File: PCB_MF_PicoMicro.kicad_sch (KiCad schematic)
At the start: 4 parts, among them J2 Conn_01x02_Pin, J7 Conn_01x02_Pin, J8 Conn_01x02_Pin, U5 ProMicro

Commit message: first changes for RP2350A
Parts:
- removed J2: Conn_01x02_Pin, Connector_JST:JST_XH_B2B-XH-A_1x02_P2.50mm_Vertical, symbol _MobiFlight:JST-XH_02_Pin_vertical

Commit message: optimazations
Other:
- sheet RP2040 renamed RP2350A
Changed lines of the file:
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@@
 			(color 0 0 0 0.0000)
 		)
-		(property "Sheetname" "RP2040"
+		(property "Sheetname" "RP2350A"
 			(at 27.94 33.5784 0)
 			(effects

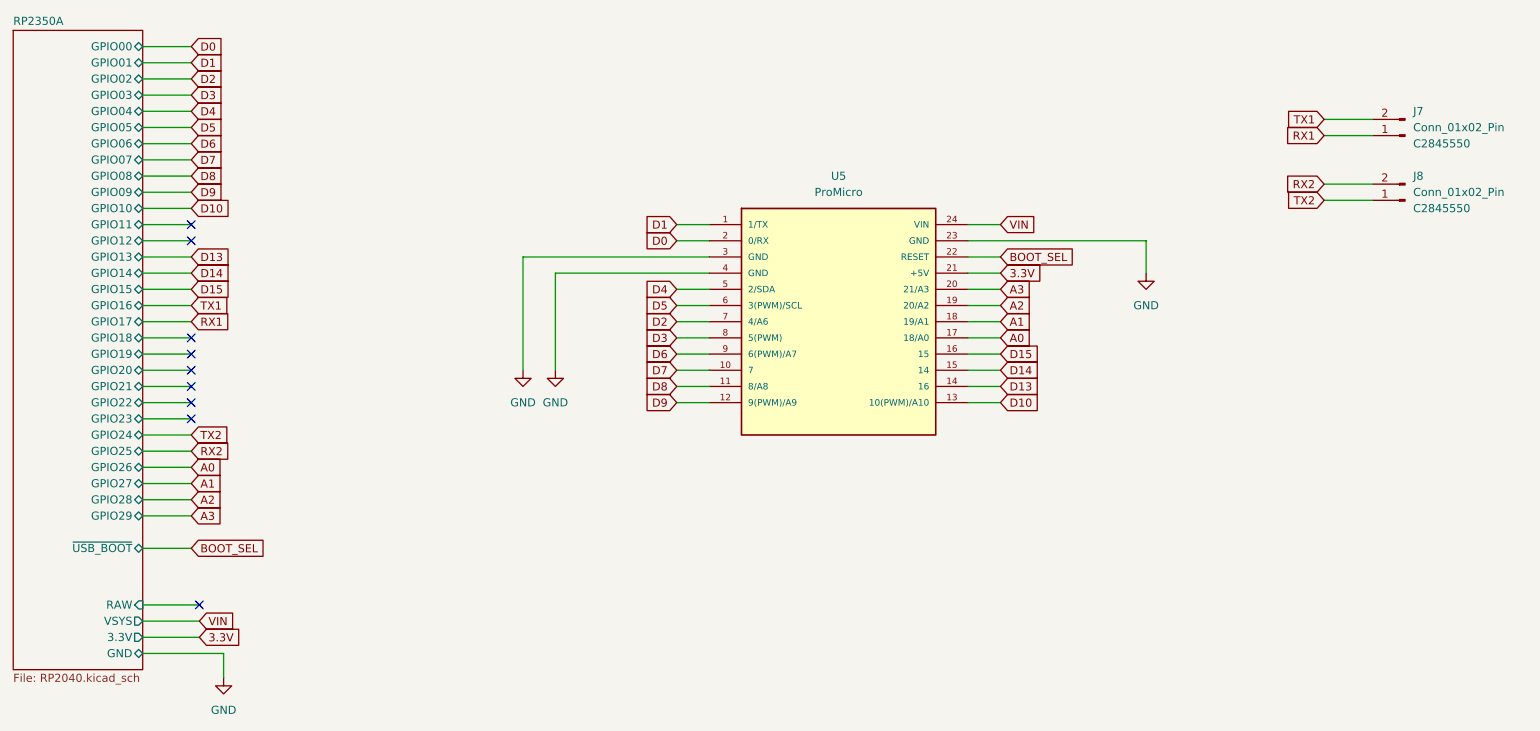
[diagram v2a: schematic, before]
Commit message: add LED, make board smaller
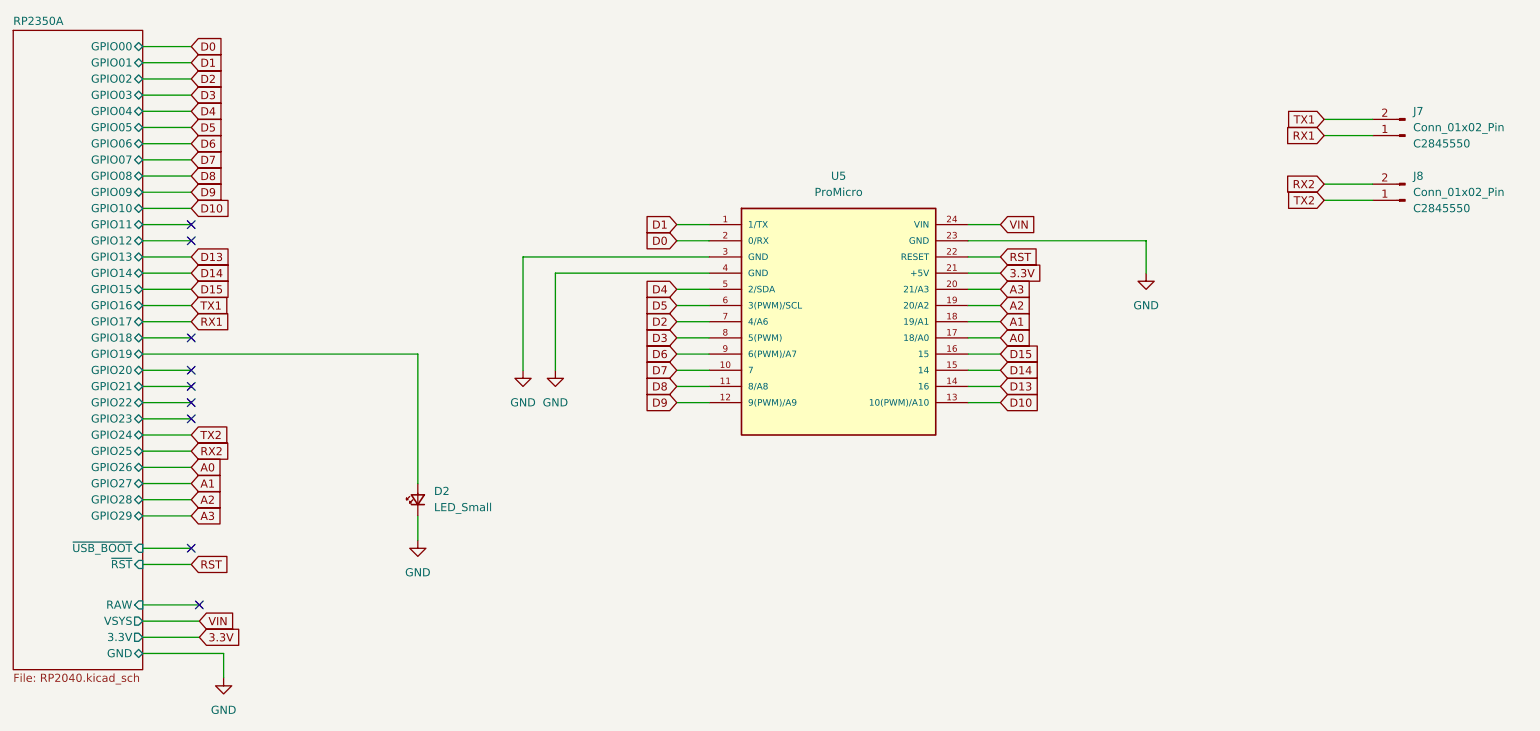
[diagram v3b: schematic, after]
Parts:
- added D2: LED_Small, LED_SMD:LED_0402_1005Metric, symbol Device:LED_Small
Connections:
- net GND: now also D2.1 (K)
- net RP2350A/GPIO19: now also D2.2 (A)
- net BOOT_SEL renamed RST
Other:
- sheet RP2350A ports: added ~{RST}; removed none
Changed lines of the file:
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@@
-	)
-	(no_connect
-		(at 55.88 85.09)
 	)
 	(no_connect
@@
 	)
 	(no_connect
+		(at 55.88 115.57)
+	)
+	(no_connect
 		(at 55.88 92.71)
 	)
@@
 	(wire
 		(pts
+			(xy 91.44 110.49) (xy 91.44 114.3)
+		)
+		(stroke
+			(width 0)
+			(type default)
+		)
+	)
+	(wire
+		(pts
 			(xy 113.03 72.39) (xy 137.16 72.39)
 		)
@@
 	(wire
 		(pts
+			(xy 91.44 85.09) (xy 91.44 105.41)
+		)
+		(stroke
+			(width 0)
+			(type default)
+		)
+	)
+	(wire
+		(pts
 			(xy 48.26 41.91) (xy 55.88 41.91)
 		)
@@
 	(wire
 		(pts
-			(xy 48.26 85.09) (xy 55.88 85.09)
+			(xy 48.26 85.09) (xy 91.44 85.09)
 		)
 		(stroke
@@
 		)
 	)
+	(wire
+		(pts
+			(xy 48.26 118.11) (xy 55.88 118.11)
+		)
+		(stroke
+			(width 0)
+			(type default)
+		)
+	)
 	(global_label "D5"
 		(shape input)
@@
 		)
 	)
+	(global_label "RST"
+		(shape input)
+		(at 55.88 118.11 0)
+		(fields_autoplaced yes)
+		(effects
+			(font
+				(size 1.27 1.27)
+			)
+			(justify left)
+		)
+		(property "Intersheetrefs" "${INTERSHEET_REFS}"
+			(at 62.3123 118.11 0)
+			(effects
+				(font
+					(size 1.27 1.27)
+				)
+				(justify left)
+				(hide yes)
+			)
+		)
+	)
 	(global_label "D7"
 		(shape input)
@@
 		)
 	)
-	(global_label "BOOT_SEL"
-		(shape input)
-		(at 55.88 115.57 0)
-		(fields_autoplaced yes)
-		(effects
-			(font
-				(size 1.27 1.27)
-			)
-			(justify left)
-		)
-		(property "Intersheetrefs" "${INTERSHEET_REFS}"
-			(at 68.118 115.57 0)
-			(effects
-				(font
-					(size 1.27 1.27)
-				)
-				(justify left)
-				(hide yes)
-			)
-		)
-	)
 	(global_label "RX2"
 		(shape input)
@@
 		)
 	)
-	(global_label "BOOT_SEL"
+	(global_label "RST"
 		(shape input)
 		(at 182.88 69.85 0)
@@
 		)
 		(property "Intersheetrefs" "${INTERSHEET_REFS}"
-			(at 195.118 69.85 0)
+			(at 189.3123 69.85 0)
 			(effects
 				(font
@@
 	)
 	(symbol
+		(lib_id "power:GND")
+		(at 91.44 114.3 0)
+		(unit 1)
+		(exclude_from_sim no)
+		(in_bom yes)
+		(on_board yes)
+		(dnp no)
+		(fields_autoplaced yes)
+		(property "Reference" "#PWR017"
+			(at 91.44 120.65 0)
+			(effects
+				(font
+					(size 1.27 1.27)
+				)
+				(hide yes)
+			)
+		)
+		(property "Value" "GND"
+			(at 91.44 119.38 0)
+			(effects
+				(font
+					(size 1.27 1.27)
+				)
+			)
+		)
+		(property "Footprint" ""
+			(at 91.44 114.3 0)
+			(effects
+				(font
+					(size 1.27 1.27)
+				)
+				(hide yes)
+			)
+		)
+		(property "Datasheet" ""
+			(at 91.44 114.3 0)
+			(effects
+				(font
+					(size 1.27 1.27)
+				)
+				(hide yes)
+			)
+		)
+		(property "Description" "Power symbol creates a global label with name \"GND\" , ground"
+			(at 91.44 114.3 0)
+			(effects
+				(font
+					(size 1.27 1.27)
+				)
+				(hide yes)
+			)
+		)
+		(pin "1"
+		)
+		(instances
+			(project "PCB_MF_PicoMicro"
+				(path "/e63e39d7-6ac0-4ffd-8aa3-1841a4541b55"
+					(reference "#PWR017")
+					(unit 1)
+				)
+			)
+		)
+	)
+	(symbol
 		(lib_id "_Own_Library:Conn_01x02_JST_ZH")
 		(at 246.38 60.96 180)
@@
 				(path "/e63e39d7-6ac0-4ffd-8aa3-1841a4541b55"
 					(reference "J8")
+					(unit 1)
+				)
+			)
+		)
+	)
+	(symbol
+		(lib_id "Device:LED_Small")
+		(at 91.44 107.95 90)
+		(unit 1)
+		(exclude_from_sim no)
+		(in_bom yes)
+		(on_board yes)
+		(dnp no)
+		(fields_autoplaced yes)
+		(property "Reference" "D2"
+			(at 93.98 106.6164 90)
+			(effects
+				(font
+					(size 1.27 1.27)
+				)
+				(justify right)
+			)
+		)
+		(property "Value" "LED_Small"
+			(at 93.98 109.1564 90)
+			(effects
+				(font
+					(size 1.27 1.27)
+				)
+				(justify right)
+			)
+		)
+		(property "Footprint" "LED_SMD:LED_0402_1005Metric"
+			(at 91.44 107.95 90)
+			(effects
+				(font
+					(size 1.27 1.27)
+				)
+				(hide yes)
+			)
+		)
+		(property "Datasheet" "~"
+			(at 91.44 107.95 90)
+			(effects
+				(font
+					(size 1.27 1.27)
+				)
+				(hide yes)
+			)
+		)
+		(property "Description" "Light emitting diode, small symbol"
+			(at 91.44 107.95 0)
+			(effects
+				(font
+					(size 1.27 1.27)
+				)
+				(hide yes)
+			)
+		)
+		(property "Sim.Pin" "1=K 2=A"
+			(at 91.44 107.95 0)
+			(effects
+				(font
+					(size 1.27 1.27)
+				)
+				(hide yes)
+			)
+		)
+		(pin "1"
+		)
+		(pin "2"
+		)
+		(instances
+			(project ""
+				(path "/e63e39d7-6ac0-4ffd-8aa3-1841a4541b55"
+					(reference "D2")
 					(unit 1)
 				)
@@
 			)
 		)
-		(pin "~{USB_BOOT}" bidirectional
+		(pin "~{USB_BOOT}" input
 			(at 48.26 115.57 0)
 			(effects
@@
 			(effects
 				(font
+					(size 1.27 1.27)
+				)
+				(justify right)
+			)
+		)
+		(pin "~{RST}" input
+			(at 48.26 118.11 0)
+			(effects
+				(font

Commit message: add 2nd LED
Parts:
- added D3: green, LED_SMD:LED_0402_1005Metric, symbol Device:LED_Small
- D2: value LED_Small -> green
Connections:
- net GND: now also D3.1 (K)
- net RP2350A/GPIO11: now also D3.2 (A)
- no-connect marks 9 -> 8
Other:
- moved on the sheet: D2
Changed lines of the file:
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@@
-	)
-	(no_connect
-		(at 55.88 64.77)
 	)
 	(no_connect
@@
 	(wire
 		(pts
-			(xy 91.44 110.49) (xy 91.44 114.3)
+			(xy 81.28 97.79) (xy 81.28 101.6)
 		)
 		(stroke
@@
 	(wire
 		(pts
+			(xy 81.28 64.77) (xy 81.28 67.31)
+		)
+		(stroke
+			(width 0)
+			(type default)
+		)
+	)
+	(wire
+		(pts
 			(xy 132.08 92.71) (xy 137.16 92.71)
 		)
@@
 	(wire
 		(pts
-			(xy 91.44 85.09) (xy 91.44 105.41)
+			(xy 81.28 85.09) (xy 81.28 92.71)
 		)
 		(stroke
@@
 	(wire
 		(pts
-			(xy 48.26 64.77) (xy 55.88 64.77)
+			(xy 48.26 64.77) (xy 81.28 64.77)
 		)
 		(stroke
@@
 	(wire
 		(pts
-			(xy 48.26 85.09) (xy 91.44 85.09)
+			(xy 48.26 85.09) (xy 81.28 85.09)
 		)
 		(stroke
@@
 		(pts
 			(xy 48.26 62.23) (xy 55.88 62.23)
+		)
+		(stroke
+			(width 0)
+			(type default)
+		)
+	)
+	(wire
+		(pts
+			(xy 81.28 72.39) (xy 81.28 76.2)
 		)
 		(stroke
@@
 	(symbol
 		(lib_id "power:GND")
-		(at 91.44 114.3 0)
+		(at 81.28 101.6 0)
 		(unit 1)
 		(exclude_from_sim no)
@@
 		(fields_autoplaced yes)
 		(property "Reference" "#PWR017"
-			(at 91.44 120.65 0)
+			(at 81.28 107.95 0)
 			(effects
 				(font
@@
 		)
 		(property "Value" "GND"
-			(at 91.44 119.38 0)
+			(at 81.28 106.68 0)
 			(effects
 				(font
@@
 		)
 		(property "Footprint" ""
-			(at 91.44 114.3 0)
+			(at 81.28 101.6 0)
 			(effects
 				(font
@@
 		)
 		(property "Datasheet" ""
-			(at 91.44 114.3 0)
+			(at 81.28 101.6 0)
 			(effects
 				(font
@@
 		)
 		(property "Description" "Power symbol creates a global label with name \"GND\" , ground"
-			(at 91.44 114.3 0)
+			(at 81.28 101.6 0)
 			(effects
 				(font
@@
 	(symbol
 		(lib_id "Device:LED_Small")
-		(at 91.44 107.95 90)
+		(at 81.28 95.25 90)
 		(unit 1)
 		(exclude_from_sim no)
@@
 		(fields_autoplaced yes)
 		(property "Reference" "D2"
-			(at 93.98 106.6164 90)
-			(effects
-				(font
-					(size 1.27 1.27)
-				)
-				(justify right)
-			)
-		)
-		(property "Value" "LED_Small"
-			(at 93.98 109.1564 90)
+			(at 83.82 93.9164 90)
+			(effects
+				(font
+					(size 1.27 1.27)
+				)
+				(justify right)
+			)
+		)
+		(property "Value" "green"
+			(at 83.82 96.4564 90)
 			(effects
 				(font
@@
 		)
 		(property "Footprint" "LED_SMD:LED_0402_1005Metric"
-			(at 91.44 107.95 90)
+			(at 81.28 95.25 90)
 			(effects
 				(font
@@
 		)
 		(property "Datasheet" "~"
-			(at 91.44 107.95 90)
+			(at 81.28 95.25 90)
 			(effects
 				(font
@@
 		)
 		(property "Description" "Light emitting diode, small symbol"
-			(at 91.44 107.95 0)
+			(at 81.28 95.25 0)
 			(effects
 				(font
@@
 		)
 		(property "Sim.Pin" "1=K 2=A"
-			(at 91.44 107.95 0)
+			(at 81.28 95.25 0)
 			(effects
 				(font
@@
 				(path "/e63e39d7-6ac0-4ffd-8aa3-1841a4541b55"
 					(reference "D2")
+					(unit 1)
+				)
+			)
+		)
+	)
+	(symbol
+		(lib_id "Device:LED_Small")
+		(at 81.28 69.85 90)
+		(unit 1)
+		(exclude_from_sim no)
+		(in_bom yes)
+		(on_board yes)
+		(dnp no)
+		(fields_autoplaced yes)
+		(property "Reference" "D3"
+			(at 83.82 68.5164 90)
+			(effects
+				(font
+					(size 1.27 1.27)
+				)
+				(justify right)
+			)
+		)
+		(property "Value" "green"
+			(at 83.82 71.0564 90)
+			(effects
+				(font
+					(size 1.27 1.27)
+				)
+				(justify right)
+			)
+		)
+		(property "Footprint" "LED_SMD:LED_0402_1005Metric"
+			(at 81.28 69.85 90)
+			(effects
+				(font
+					(size 1.27 1.27)
+				)
+				(hide yes)
+			)
+		)
+		(property "Datasheet" "~"
+			(at 81.28 69.85 90)
+			(effects
+				(font
+					(size 1.27 1.27)
+				)
+				(hide yes)
+			)
+		)
+		(property "Description" "Light emitting diode, small symbol"
+			(at 81.28 69.85 0)
+			(effects
+				(font
+					(size 1.27 1.27)
+				)
+				(hide yes)
+			)
+		)
+		(property "Sim.Pin" "1=K 2=A"
+			(at 81.28 69.85 0)
+			(effects
+				(font
+					(size 1.27 1.27)
+				)
+				(hide yes)
+			)
+		)
+		(pin "1"
+		)
+		(pin "2"
+		)
+		(instances
+			(project "PCB_MF_PicoMicro"
+				(path "/e63e39d7-6ac0-4ffd-8aa3-1841a4541b55"
+					(reference "D3")
 					(unit 1)
 				)
@@
 					(unit 1)
 				)
+			)
+		)
+	)
+	(symbol
+		(lib_id "power:GND")
+		(at 81.28 76.2 0)
+		(unit 1)
+		(exclude_from_sim no)
+		(in_bom yes)
+		(on_board yes)
+		(dnp no)
+		(fields_autoplaced yes)
+		(property "Reference" "#PWR018"
+			(at 81.28 82.55 0)
+			(effects
+				(font
+					(size 1.27 1.27)
+				)
+				(hide yes)
+			)
+		)
+		(property "Value" "GND"
+			(at 81.28 81.28 0)
+			(effects
+				(font
+					(size 1.27 1.27)
+				)
+			)
+		)
+		(property "Footprint" ""
+			(at 81.28 76.2 0)
+			(effects
+				(font
+					(size 1.27 1.27)
+				)
+				(hide yes)
+			)
+		)
+		(property "Datasheet" ""
+			(at 81.28 76.2 0)
+			(effects
+				(font
+					(size 1.27 1.27)
+				)
+				(hide yes)
+			)
+		)
+		(property "Description" "Power symbol creates a global label with name \"GND\" , ground"
+			(at 81.28 76.2 0)
+			(effects
+				(font
+					(size 1.27 1.27)
+				)
+				(hide yes)
+			)
+		)
+		(pin "1"
+		)
+		(instances
+			(project "PCB_MF_PicoMicro"
+				(path "/e63e39d7-6ac0-4ffd-8aa3-1841a4541b55"
+					(reference "#PWR018")
+					(unit 1)
+				)
